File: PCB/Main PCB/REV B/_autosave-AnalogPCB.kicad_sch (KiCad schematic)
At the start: 77 parts, among them J1 DF12NB_4.0_-20DP-0.5V_51_, J2 393570002, J3 393570002, J4 393570002, J5 393570002, J6 SJ3-35053D, Q1 2N7002, Q2 2N7002, Q3 2N7002, U1 ALDP105W, U2 ALDP105W, U3 ALDP105W

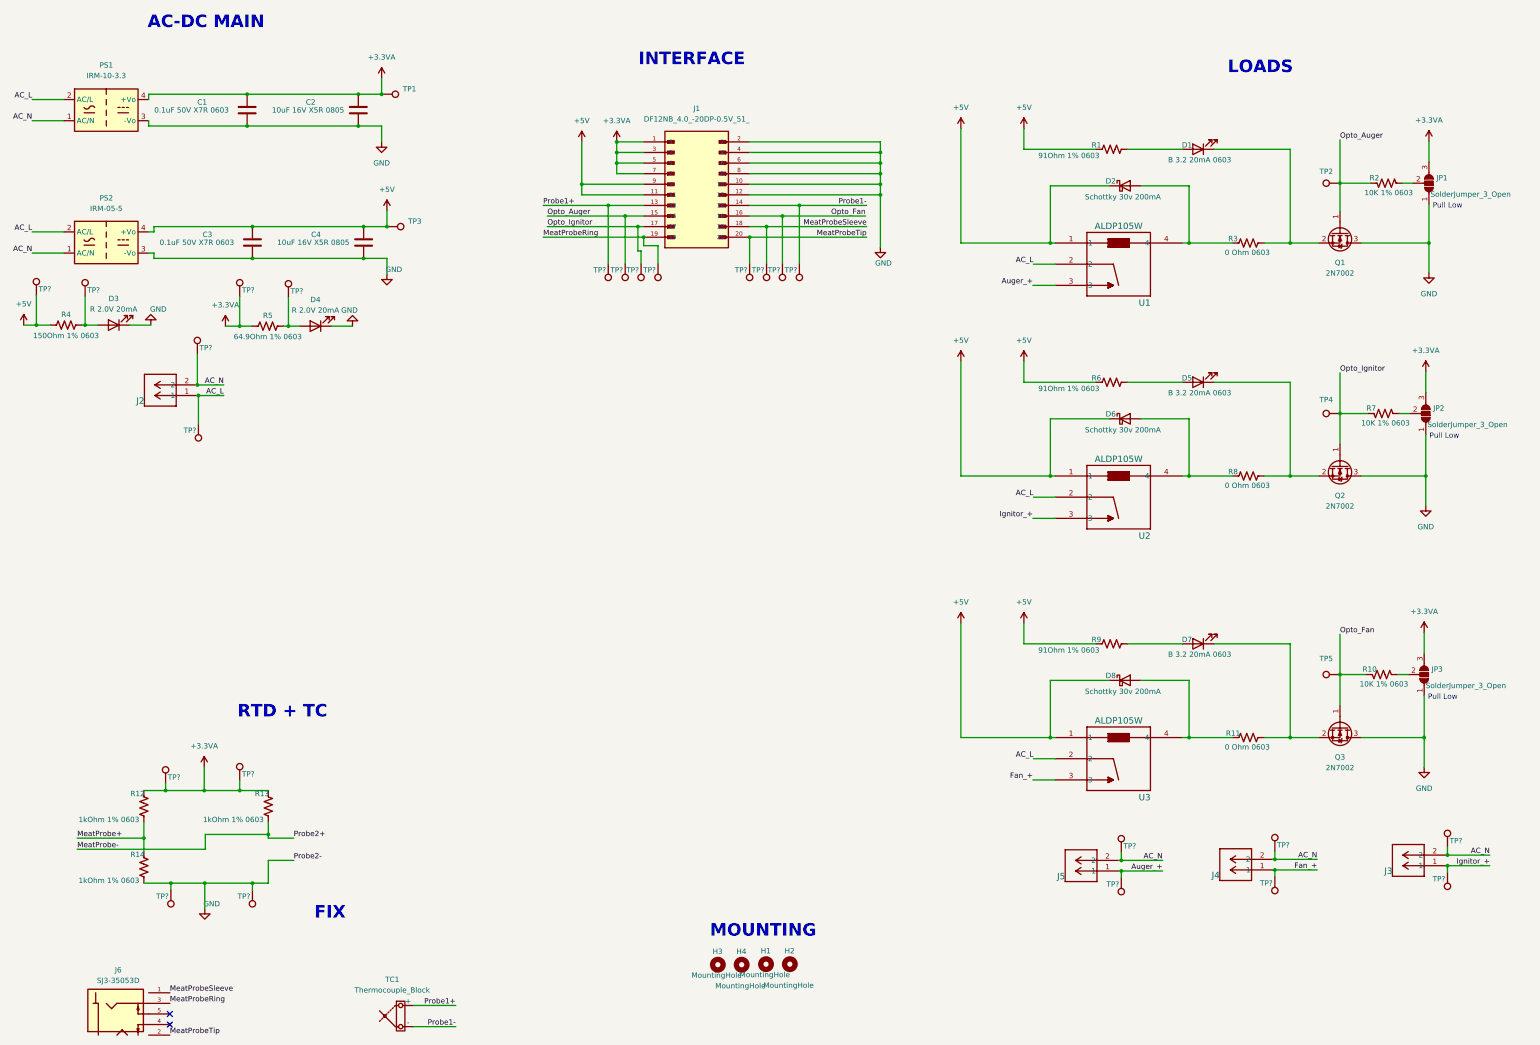
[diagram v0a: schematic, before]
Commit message: PCB - Lay out analog led and power filtering
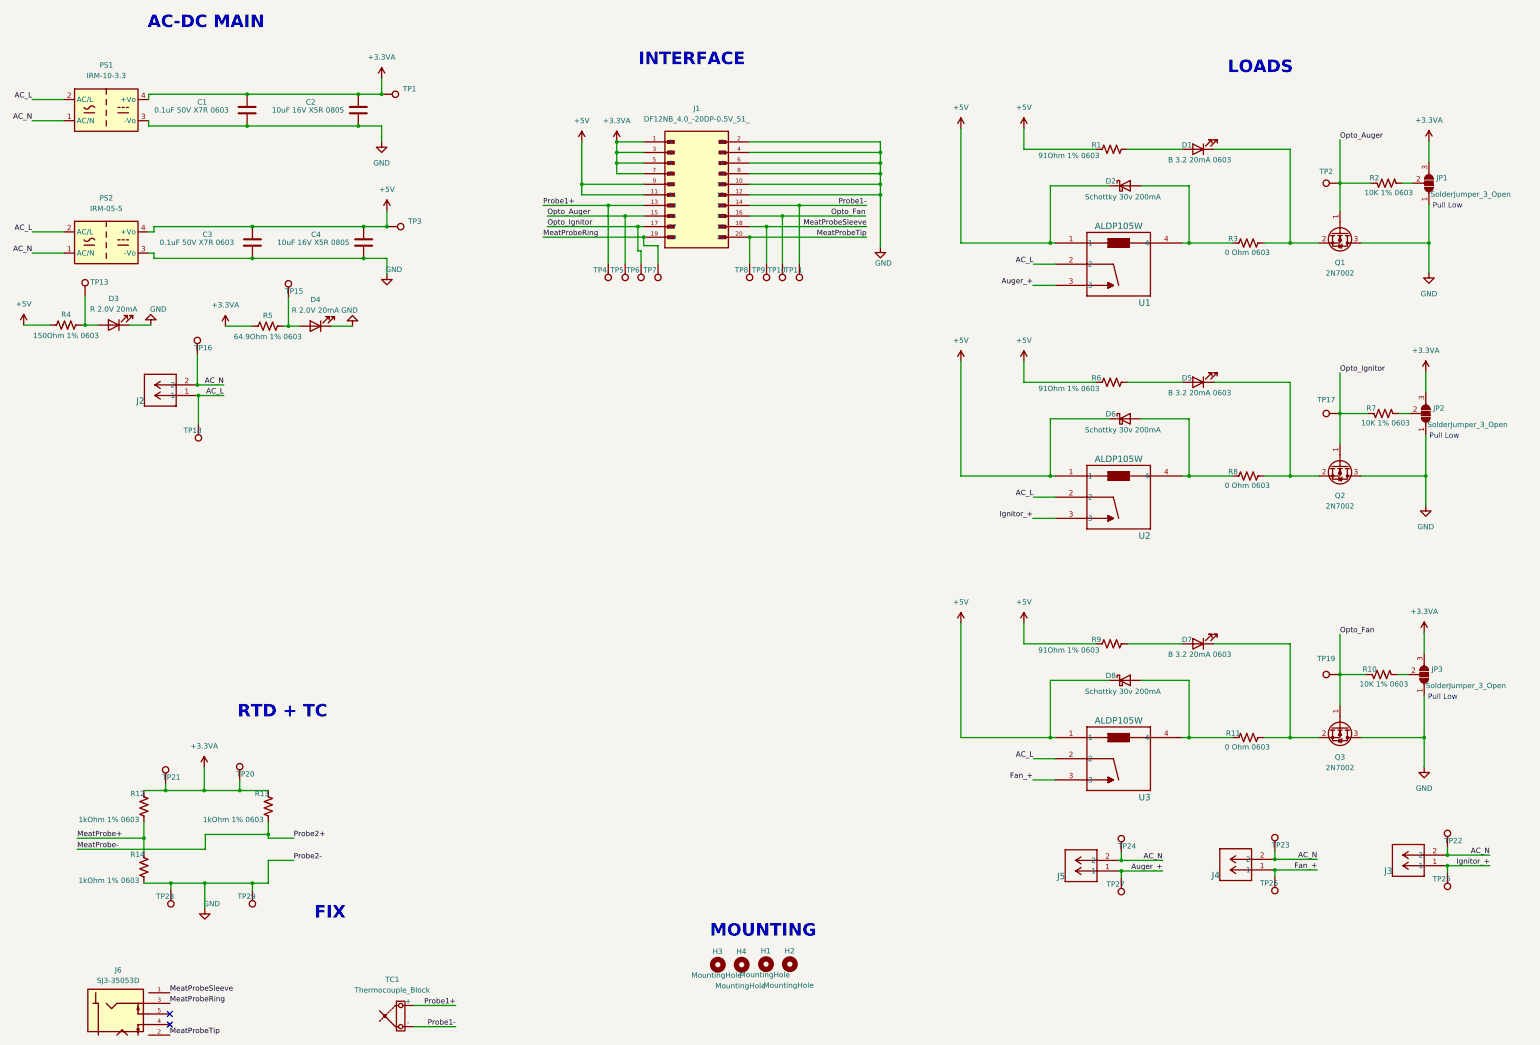
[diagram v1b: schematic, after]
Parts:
- removed TP? (x2): TP, TestPoint:TestPoint_Pad_D1.0mm, symbol Connector:TestPoint
- gave numbers to parts that had none: 22
- renumbered TP4 to TP17, TP5 to TP19

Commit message: PCB - Lay out analog mostly complete. cad added
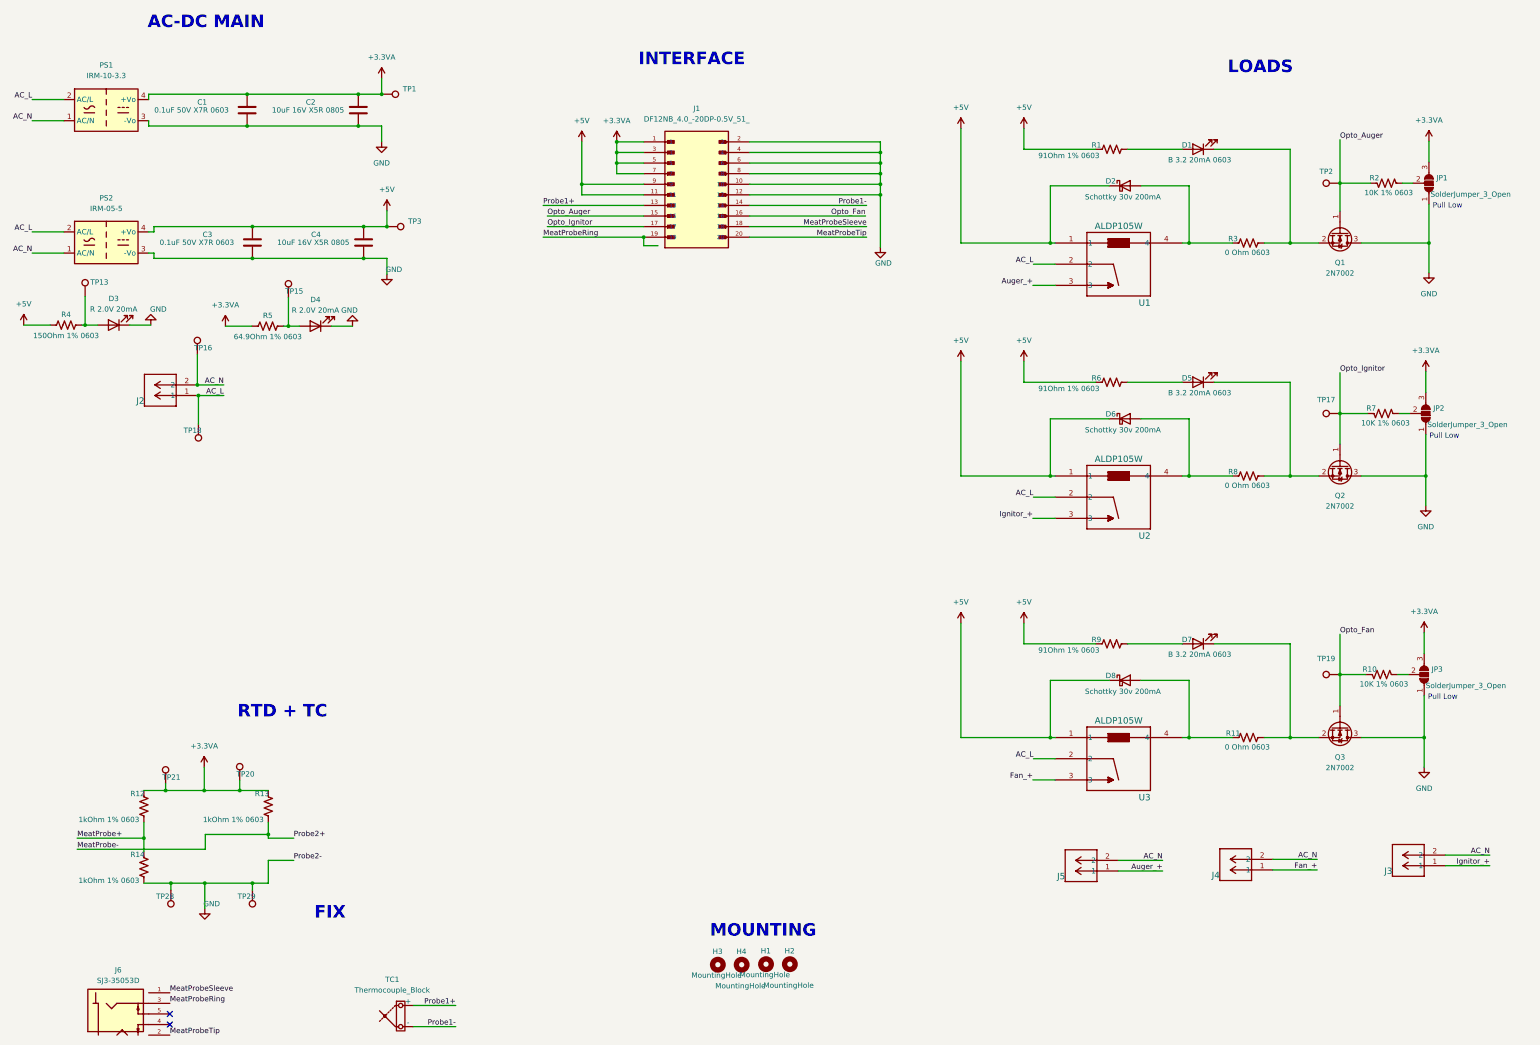
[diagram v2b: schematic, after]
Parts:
- removed TP10, TP11, TP22, TP23, TP24, TP25, TP26, TP27, TP4, TP5, TP6, TP7, TP8, TP9: TP, TestPoint:TestPoint_Pad_D1.0mm, symbol Connector:TestPoint
